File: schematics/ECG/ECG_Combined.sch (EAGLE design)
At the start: 66 parts, among them IC1 ADS1293, IC2 LIS3DH, IC3 MCP1703, IC4 CC2541, IC5 FSA4157, IC6 FSA4157, IC7 FSA4157, X1 XTAL-2SMD, X2 XTAL_403, X3 XTAL-CSM7

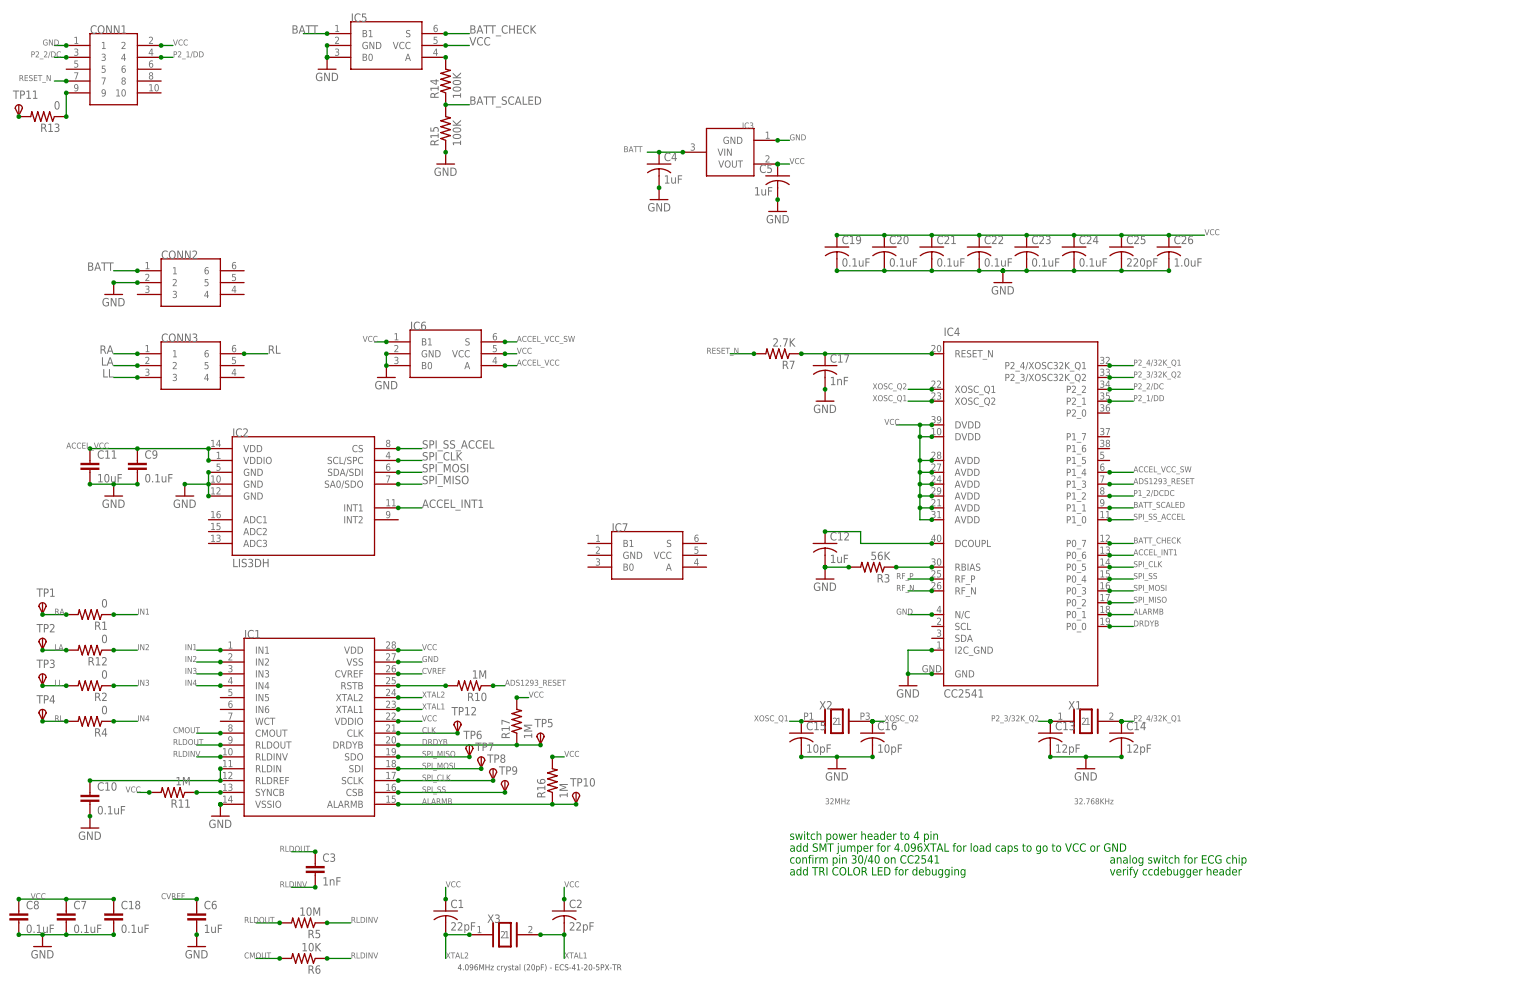
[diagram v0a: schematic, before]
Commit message: added analog switch for ads1293 power. added jumper for ads1293 xtal gnd/vcc connection
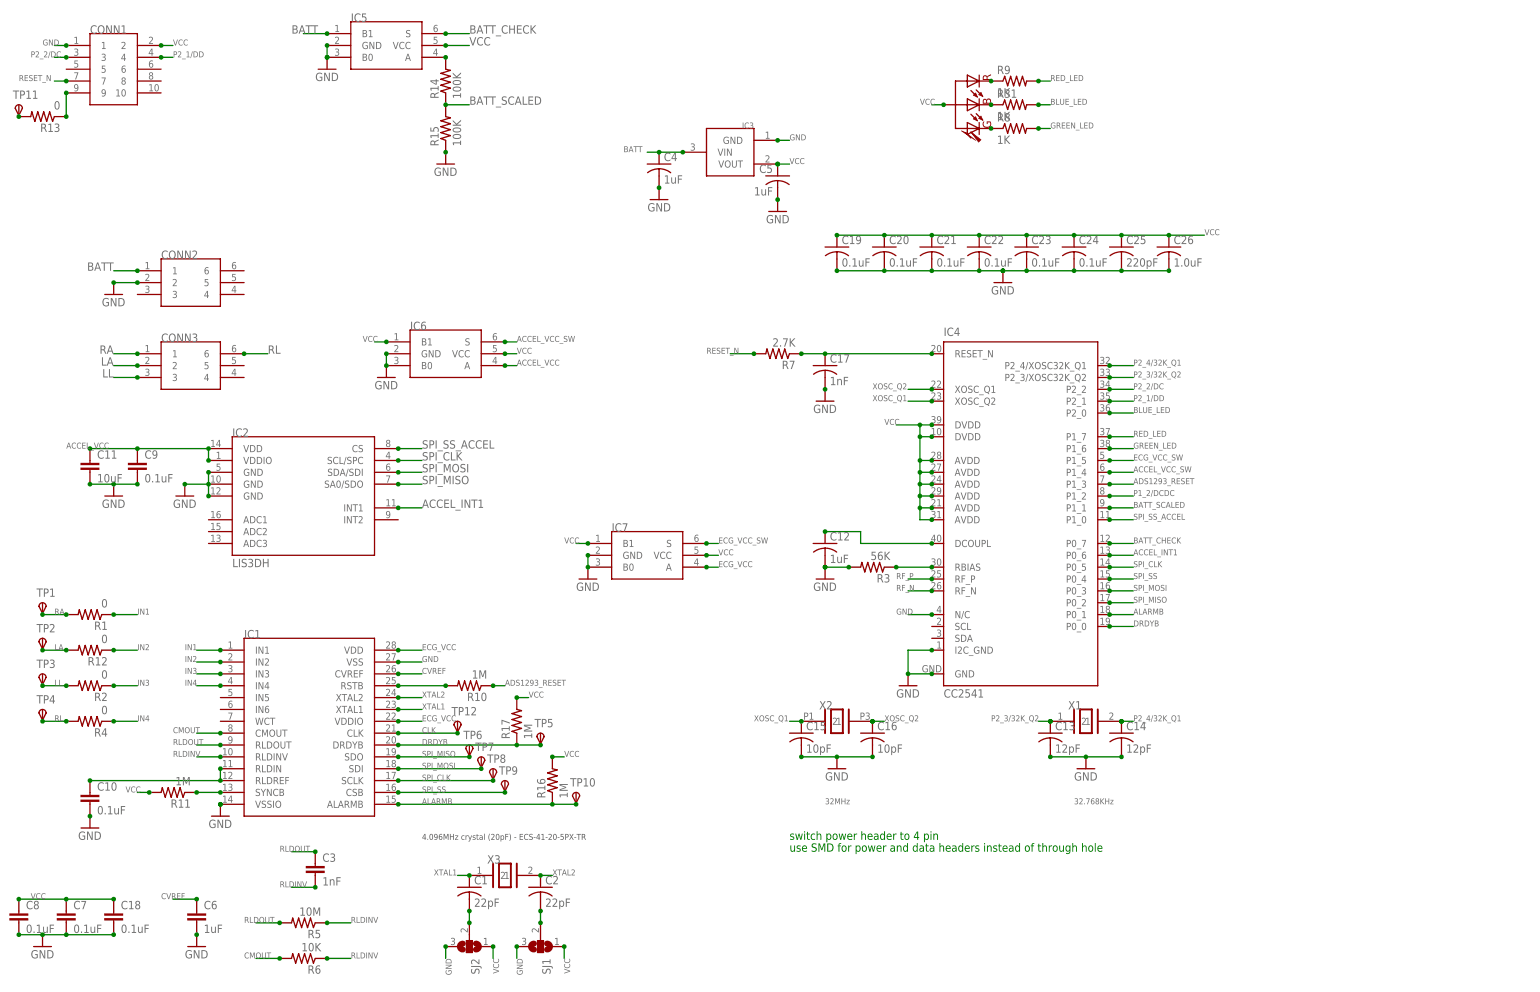
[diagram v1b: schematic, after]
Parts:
- added R31, R8, R9: 1K, rcl:R-US_R0402
- added SJ1, SJ2: (no value), jumper:SJ2W
- added TRI_LED: SML-LX0404SIUPGUSB, lumex:SML-LX0404SIUPGUSB
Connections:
- new net BLUE_LED: IC4.P2_0, R31.2
- new net ECG_VCC: IC1.VDD, IC1.VDDIO, IC7.A
- new net ECG_VCC_SW: IC4.P1_5, IC7.S
- new net GREEN_LED: IC4.P1_6, R8.2
- new net N$10: C2.2, SJ1.2
- new net N$13: C1.2, SJ2.2
- new net N$20: R8.1, TRI_LED.R
- new net N$3: R9.1, TRI_LED.B
- new net N$9: R31.1, TRI_LED.G
- new net RED_LED: IC4.P1_7, R9.2
- net GND: now also IC7.B0, IC7.GND, SJ1.3, SJ2.3
- net VCC: now also IC7.B1, IC7.VCC, SJ1.1, SJ2.1, TRI_LED.A; no longer C1.1, C2.1, IC1.VDD, IC1.VDDIO
- net XTAL1: now also C1.1, X3.1; no longer C2.2, X3.2
- net XTAL2: now also C2.1, X3.2; no longer C1.2, X3.1
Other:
- note added: "use SMD for power and data headers instead of through hole"
- note removed: "add SMT jumper for 4.096XTAL for load caps to go to VCC or GND"
- note removed: "add TRI COLOR LED for debugging"
- note removed: "analog switch for ECG chip"
- note removed: "confirm pin 30/40 on CC2541"
- note removed: "verify ccdebugger header"
- moved on the sheet: C1, C2, X3

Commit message: replaced 6 pin power header with 4 pin. added ESD protection diodes to circuit input
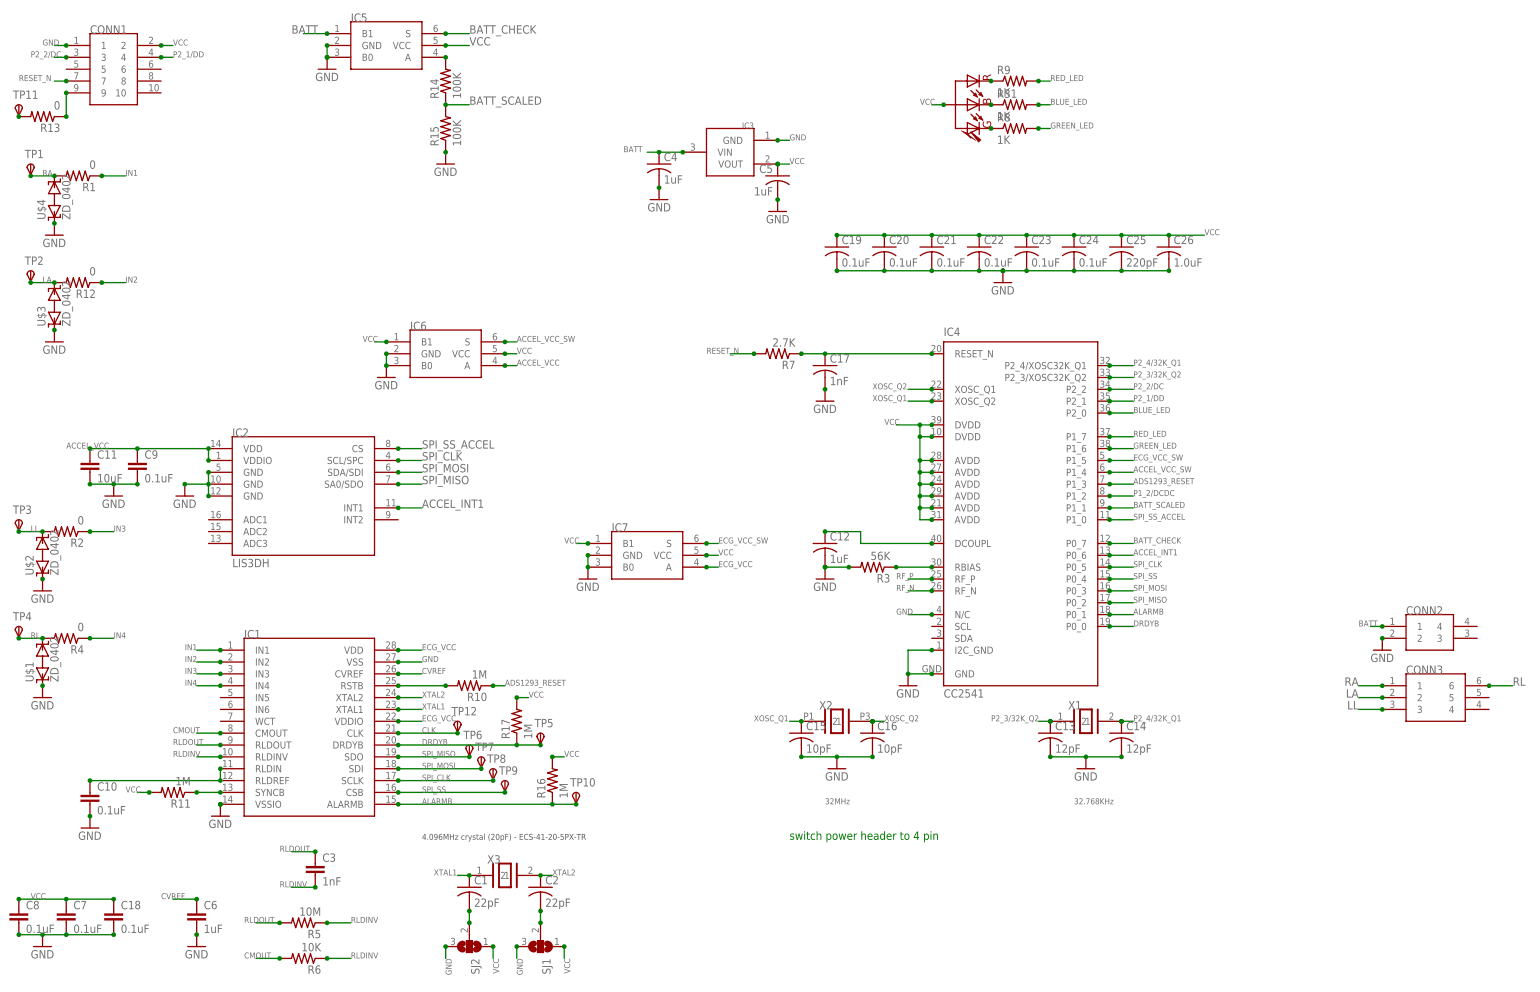
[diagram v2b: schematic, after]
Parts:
- added U$1, U$2, U$3, U$4: ZD_0402, semtech:ZD_0402
- CONN2: value M80-6V -> M80-4V; device harwin:M80-6V -> harwin:M80-4V
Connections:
- net GND: now also U$1.A, U$2.A, U$3.A, U$4.A
- net LA: now also U$3.C
- net LL: now also U$2.C
- net RA: now also U$4.C
- net RL: now also U$1.C
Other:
- note removed: "use SMD for power and data headers instead of through hole"
- moved on the sheet: CONN3, R1, R12, R2, R4, TP1, TP2, TP3, TP4
